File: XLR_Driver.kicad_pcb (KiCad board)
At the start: 2 copper layers, 50 x 30 mm, 36 parts, among them IC1 LM317L_SO8, IC2 LM337L_SO8, IC3 DRV134UA, J1 Conn_01x02_Male, J2 Conn_01x02_Male, P1 Conn_01x03_Male, P2 Conn_01x06_Male, P3 Conn_01x02_Male

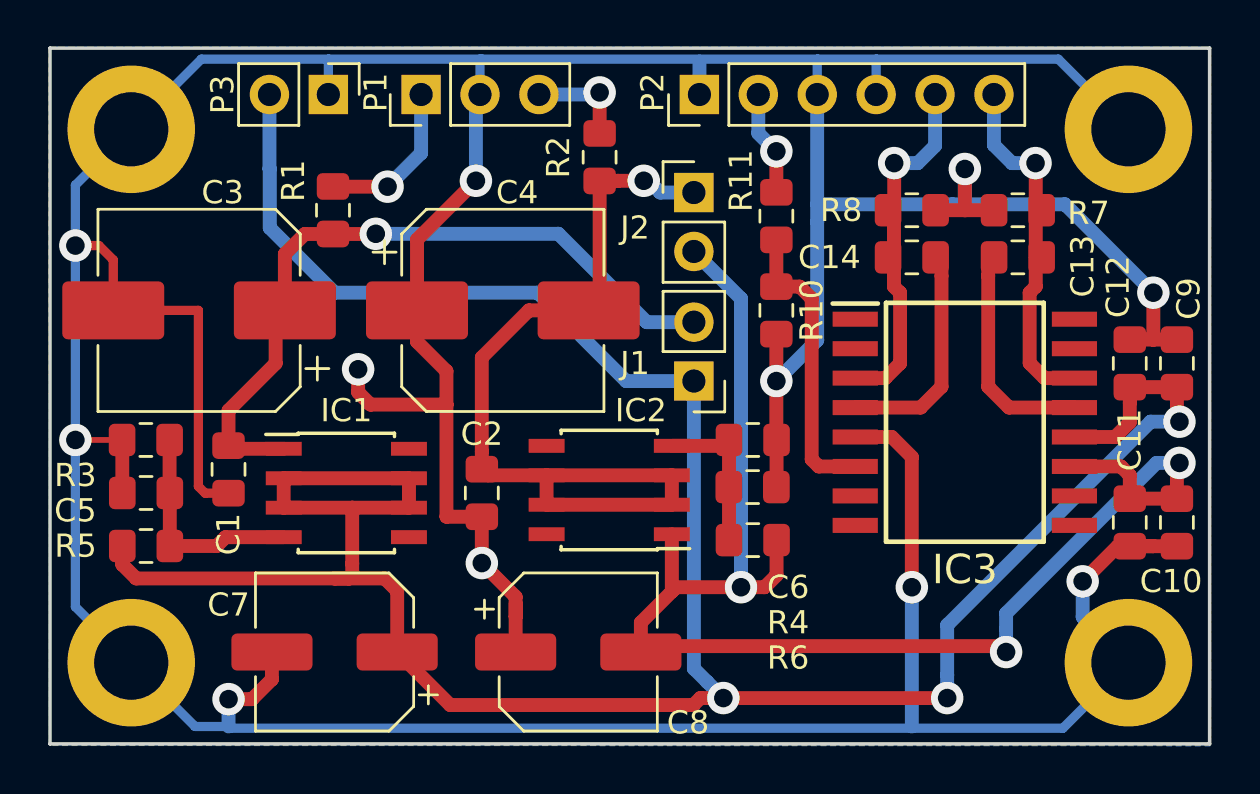
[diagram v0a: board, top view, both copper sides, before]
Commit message: V1.0 release
Completed circuit 
Ready to order PCBs
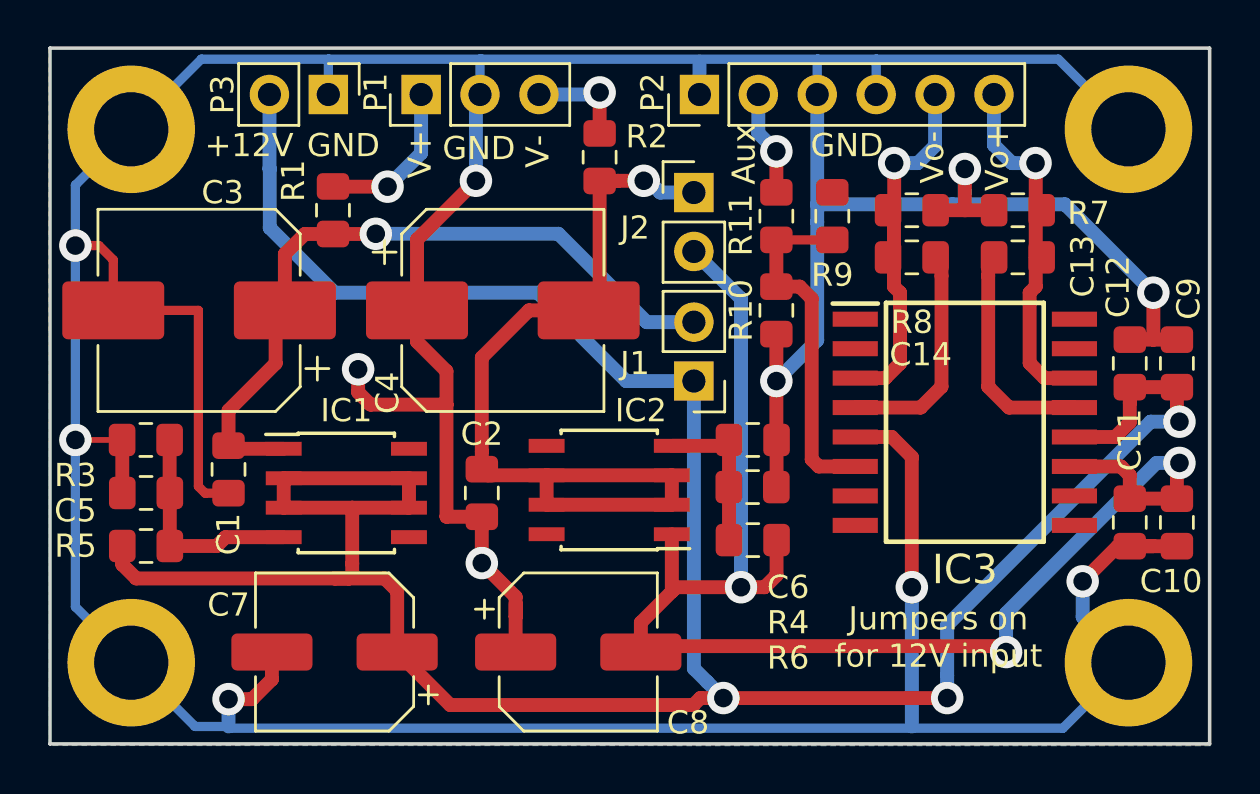
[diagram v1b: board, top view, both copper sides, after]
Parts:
- added R9: R, Resistor_SMD:R_0805_2012Metric_Pad1.15x1.40mm_HandSolder, F.Cu at (133.7, 47.2)
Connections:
- net /? renamed Net-(IC3-Pad6)
- IC1 pad 5: (no net) -> Net-(IC1-Pad5)
- IC1 pad 8: (no net) -> Net-(IC1-Pad8)
- IC2 pad 5: (no net) -> Net-(IC2-Pad5)
- IC2 pad 8: (no net) -> Net-(IC2-Pad8)
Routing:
- net Net-(IC3-Pad6): track 12.7 -> 15.1 mm
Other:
- board text added: "+12V"
- board text added: "Aux"
- board text added: "GND"
- board text added: "Jumpers on for 12V input"
- board text added: "V+"
- board text added: "V-"
- board text added: "Vo+"
- board text added: "Vo-"
